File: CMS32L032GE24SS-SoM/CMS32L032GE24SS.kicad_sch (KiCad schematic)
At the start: 9 parts, among them J101 MCU Right Side, J102 MCU Left Side, U101 CMS32L032GE24SS

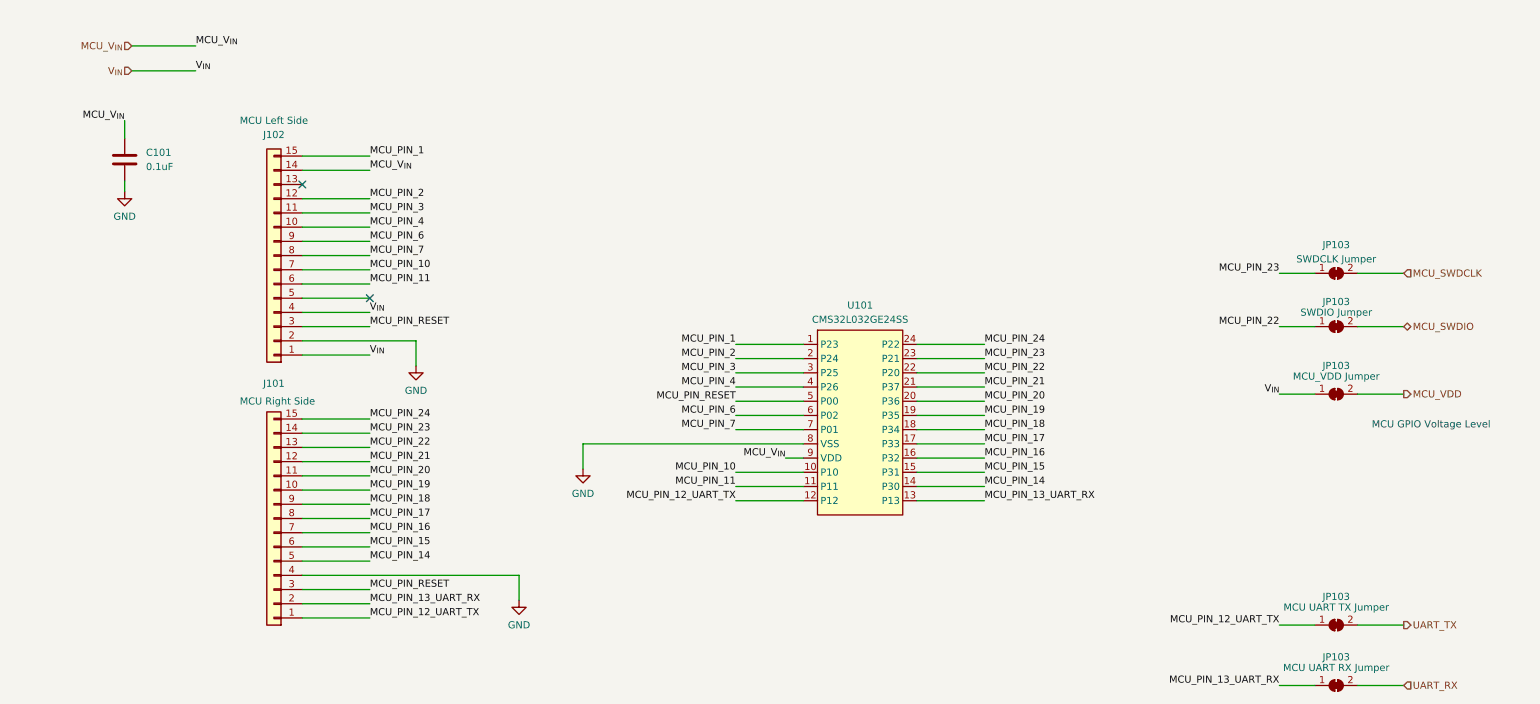
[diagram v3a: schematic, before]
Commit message: changed Power Source jumpers
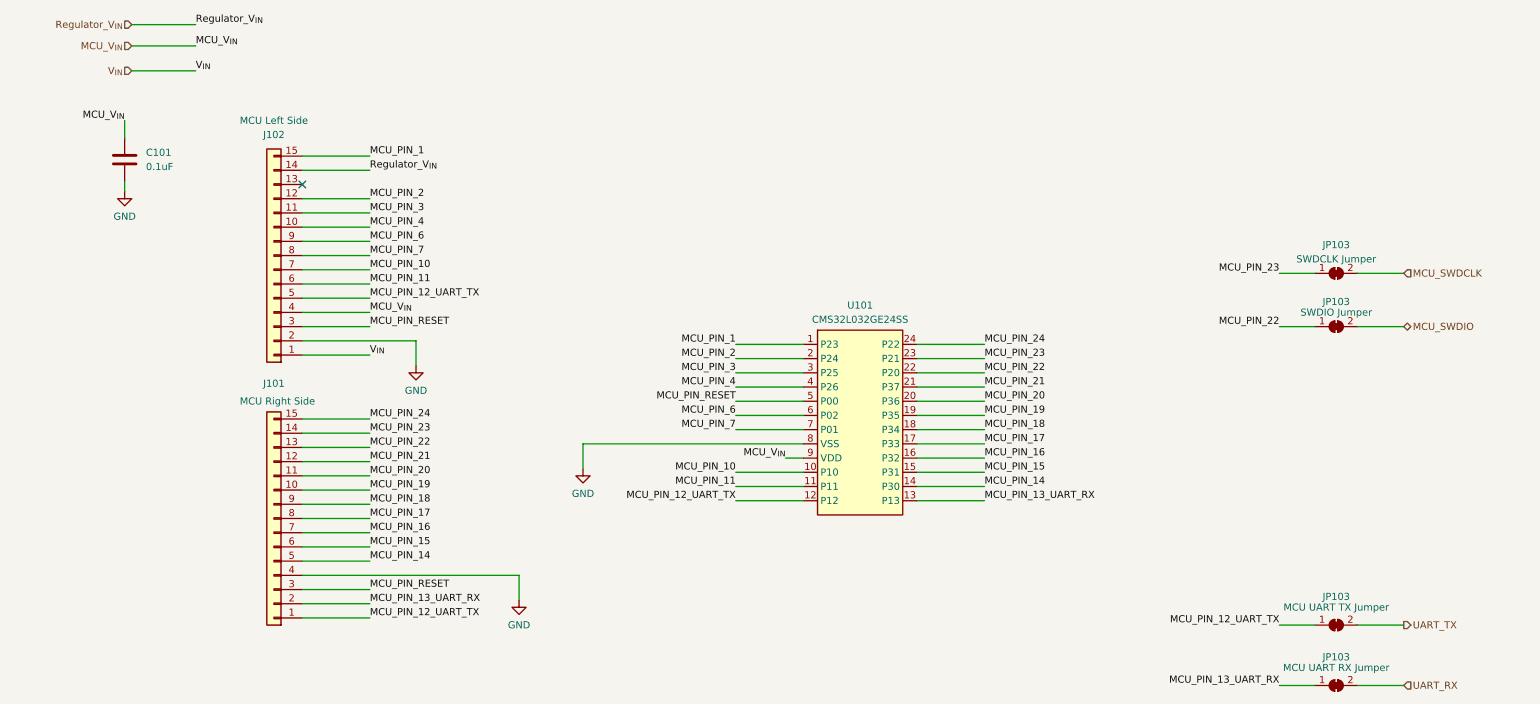
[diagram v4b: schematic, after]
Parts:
- removed JP103: MCU_VDD Jumper, Jumper:SolderJumper-2_P1.3mm_Bridged_RoundedPad1.0x1.5mm, symbol Jumper:SolderJumper_2_Bridged
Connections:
- net MCU_PIN_12_UART_TX: now also J102.5 (Pin_5)
- net MCU_V_{IN}: now also J102.4 (Pin_4); no longer J102.14 (Pin_14)
- net V_{IN}: no longer J102.4 (Pin_4)
- new net Regulator_V_{IN}: J102.14 (Pin_14)
- no-connect marks 2 -> 1
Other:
- note removed: "MCU GPIO Voltage Level"
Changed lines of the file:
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@@
 (kicad_sch (version 20230121) (generator eeschema)
   (paper "A4")
-  (no_connect (at 71.12 69.85))
   (no_connect (at 59.055 49.53))
   (wire (pts (xy 59.055 74.93) (xy 71.12 74.93))
@@
     (stroke (width 0) (type default))
   )
-  (wire (pts (xy 247.65 86.995) (xy 255.905 86.995))
-    (stroke (width 0) (type default))
-  )
   (wire (pts (xy 59.055 67.31) (xy 71.12 67.31))
     (stroke (width 0) (type default))
@@
     (stroke (width 0) (type default))
   )
+  (wire (pts (xy 28.575 20.955) (xy 40.005 20.955))
+    (stroke (width 0) (type default))
+  )
   (wire (pts (xy 59.055 72.39) (xy 71.12 72.39))
     (stroke (width 0) (type default))
@@
     (stroke (width 0) (type default))
   )
-  (wire (pts (xy 233.68 86.995) (xy 240.03 86.995))
-    (stroke (width 0) (type default))
-  )
   (wire (pts (xy 168.91 83.185) (xy 180.975 83.185))
     (stroke (width 0) (type default))
@@
     (stroke (width 0) (type default))
   )
-  (text "MCU GPIO Voltage Level" (at 250.19 93.345 0)
-    (effects (font (size 1.27 1.27)) (justify left bottom))
-  )
   (label "MCU_PIN_3" (at 136.525 83.185 180) (fields_autoplaced)
     (effects (font (size 1.27 1.27)) (justify right bottom))
@@
     (effects (font (size 1.27 1.27)) (justify left bottom))
   )
-  (label "V_{IN}" (at 233.68 86.995 180) (fields_autoplaced)
-    (effects (font (size 1.27 1.27)) (justify right bottom))
-  )
   (label "MCU_PIN_7" (at 71.12 62.23 0) (fields_autoplaced)
     (effects (font (size 1.27 1.27)) (justify left bottom))
@@
     (effects (font (size 1.27 1.27)) (justify left bottom))
   )
-  (label "V_{IN}" (at 71.12 72.39 0) (fields_autoplaced)
+  (label "MCU_V_{IN}" (at 71.12 72.39 0) (fields_autoplaced)
     (effects (font (size 1.27 1.27)) (justify left bottom))
   )
@@
     (effects (font (size 1.27 1.27)) (justify left bottom))
   )
+  (label "Regulator_V_{IN}" (at 40.005 20.955 0) (fields_autoplaced)
+    (effects (font (size 1.27 1.27)) (justify left bottom))
+  )
   (label "MCU_PIN_22" (at 180.975 83.185 0) (fields_autoplaced)
     (effects (font (size 1.27 1.27)) (justify left bottom))
@@
     (effects (font (size 1.27 1.27)) (justify right bottom))
   )
-  (label "MCU_V_{IN}" (at 71.12 46.99 0) (fields_autoplaced)
+  (label "Regulator_V_{IN}" (at 71.12 46.99 0) (fields_autoplaced)
     (effects (font (size 1.27 1.27)) (justify left bottom))
   )
@@
   )
   (label "MCU_PIN_21" (at 71.12 99.06 0) (fields_autoplaced)
+    (effects (font (size 1.27 1.27)) (justify left bottom))
+  )
+  (label "MCU_PIN_12_UART_TX" (at 71.12 69.85 0) (fields_autoplaced)
     (effects (font (size 1.27 1.27)) (justify left bottom))
   )
@@
     (effects (font (size 1.27 1.27)) (justify left))
   )
-  (hierarchical_label "MCU_VDD" (shape output) (at 255.905 86.995 0) (fields_autoplaced)
-    (effects (font (size 1.27 1.27)) (justify left))
-  )
   (hierarchical_label "UART_RX" (shape input) (at 255.905 139.065 0) (fields_autoplaced)
     (effects (font (size 1.27 1.27)) (justify left))
@@
   (hierarchical_label "MCU_SWDCLK" (shape input) (at 255.905 65.405 0) (fields_autoplaced)
     (effects (font (size 1.27 1.27)) (justify left))
+  )
+  (hierarchical_label "Regulator_V_{IN}" (shape input) (at 28.575 20.955 180) (fields_autoplaced)
+    (effects (font (size 1.27 1.27)) (justify right))
   )
   (hierarchical_label "V_{IN}" (shape input) (at 28.575 29.21 180) (fields_autoplaced)
@@
       (effects (font (size 1.27 1.27)) hide)
     )
+    (property "Description" "" (at 27.305 45.085 0)
+      (effects (font (size 1.27 1.27)) hide)
+    )
+    (property "LCSC" "" (at 27.305 45.085 0)
+      (effects (font (size 1.27 1.27)) hide)
+    )
+    (property "Vendor" "" (at 27.305 45.085 0)
+      (effects (font (size 1.27 1.27)) hide)
+    )
+    (property "Vendor Model" "" (at 27.305 45.085 0)
+      (effects (font (size 1.27 1.27)) hide)
+    )
     (pin "1")
     (pin "2")
@@
       (effects (font (size 1.27 1.27)) hide)
     )
+    (property "Description" "" (at 243.84 74.93 0)
+      (effects (font (size 1.27 1.27)) hide)
+    )
+    (property "LCSC" "" (at 243.84 74.93 0)
+      (effects (font (size 1.27 1.27)) hide)
+    )
+    (property "Vendor" "" (at 243.84 74.93 0)
+      (effects (font (size 1.27 1.27)) hide)
+    )
+    (property "Vendor Model" "" (at 243.84 74.93 0)
+      (effects (font (size 1.27 1.27)) hide)
+    )
     (pin "1")
     (pin "2")
@@
     )
     (property "Datasheet" "~" (at 53.975 109.22 0)
+      (effects (font (size 1.27 1.27)) hide)
+    )
+    (property "Description" "" (at 53.975 109.22 0)
+      (effects (font (size 1.27 1.27)) hide)
+    )
+    (property "LCSC" "" (at 53.975 109.22 0)
+      (effects (font (size 1.27 1.27)) hide)
+    )
+    (property "Vendor" "" (at 53.975 109.22 0)
+      (effects (font (size 1.27 1.27)) hide)
+    )
+    (property "Vendor Model" "" (at 53.975 109.22 0)
       (effects (font (size 1.27 1.27)) hide)
     )
@@
     )
     (property "Datasheet" "https://www.mcu.com.cn/uploads/img1/tupian/CMS32L032%20Datasheet_V1.0.1.pdf" (at 161.29 116.205 0)
+      (effects (font (size 1.27 1.27)) hide)
+    )
+    (property "Description" "" (at 158.75 90.805 0)
+      (effects (font (size 1.27 1.27)) hide)
+    )
+    (property "LCSC" "" (at 158.75 90.805 0)
+      (effects (font (size 1.27 1.27)) hide)
+    )
+    (property "Vendor" "" (at 158.75 90.805 0)
+      (effects (font (size 1.27 1.27)) hide)
+    )
+    (property "Vendor Model" "" (at 158.75 90.805 0)
       (effects (font (size 1.27 1.27)) hide)
     )
@@
       (effects (font (size 1.27 1.27)) hide)
     )
+    (property "Description" "" (at 243.84 65.405 0)
+      (effects (font (size 1.27 1.27)) hide)
+    )
+    (property "LCSC" "" (at 243.84 65.405 0)
+      (effects (font (size 1.27 1.27)) hide)
+    )
+    (property "Vendor" "" (at 243.84 65.405 0)
+      (effects (font (size 1.27 1.27)) hide)
+    )
+    (property "Vendor Model" "" (at 243.84 65.405 0)
+      (effects (font (size 1.27 1.27)) hide)
+    )
     (pin "1")
     (pin "2")
@@
       (effects (font (size 1.27 1.27)) hide)
     )
+    (property "Description" "" (at 243.84 128.27 0)
+      (effects (font (size 1.27 1.27)) hide)
+    )
+    (property "LCSC" "" (at 243.84 128.27 0)
+      (effects (font (size 1.27 1.27)) hide)
+    )
+    (property "Vendor" "" (at 243.84 128.27 0)
+      (effects (font (size 1.27 1.27)) hide)
+    )
+    (property "Vendor Model" "" (at 243.84 128.27 0)
+      (effects (font (size 1.27 1.27)) hide)
+    )
     (pin "1")
     (pin "2")
@@
         (path "/c0ebcd8e-c90a-40d9-842d-ee55e79d6adf/29b9f769-3d76-4235-af85-93dac208c17b"
           (reference "JP204") (unit 1)
-        )
-      )
-    )
-  )
-  (symbol (lib_id "Jumper:SolderJumper_2_Bridged") (at 243.84 86.995 0) (unit 1)
-    (in_bom yes) (on_board yes) (dnp no)
-    (property "Reference" "JP103" (at 243.84 81.915 0)
-      (effects (font (size 1.27 1.27)))
-    )
-    (property "Value" "MCU_VDD Jumper" (at 243.84 83.82 0)
-      (effects (font (size 1.27 1.27)))
-    )
-    (property "Footprint" "Jumper:SolderJumper-2_P1.3mm_Bridged_RoundedPad1.0x1.5mm" (at 243.84 86.995 0)
-      (effects (font (size 1.27 1.27)) hide)
-    )
-    (property "Datasheet" "~" (at 243.84 86.995 0)
-      (effects (font (size 1.27 1.27)) hide)
-    )
-    (pin "1")
-    (pin "2")
-    (instances
-      (project "CMS32L032GE24SS-SoM"
-        (path "/c0ebcd8e-c90a-40d9-842d-ee55e79d6adf"
-          (reference "JP103") (unit 1)
-        )
-        (path "/c0ebcd8e-c90a-40d9-842d-ee55e79d6adf/29b9f769-3d76-4235-af85-93dac208c17b"
-          (reference "JP203") (unit 1)
         )
       )
@@
     )
     (property "Datasheet" "~" (at 53.975 62.23 0)
+      (effects (font (size 1.27 1.27)) hide)
+    )
+    (property "Description" "" (at 53.975 62.23 0)
+      (effects (font (size 1.27 1.27)) hide)
+    )
+    (property "LCSC" "" (at 53.975 62.23 0)
+      (effects (font (size 1.27 1.27)) hide)
+    )
+    (property "Vendor" "" (at 53.975 62.23 0)
+      (effects (font (size 1.27 1.27)) hide)
+    )
+    (property "Vendor Model" "" (at 53.975 62.23 0)
       (effects (font (size 1.27 1.27)) hide)
     )
@@
       (effects (font (size 1.27 1.27)) hide)
     )
+    (property "Description" "" (at 243.84 139.065 0)
+      (effects (font (size 1.27 1.27)) hide)
+    )
+    (property "LCSC" "" (at 243.84 139.065 0)
+      (effects (font (size 1.27 1.27)) hide)
+    )
+    (property "Vendor" "" (at 243.84 139.065 0)
+      (effects (font (size 1.27 1.27)) hide)
+    )
+    (property "Vendor Model" "" (at 243.84 139.065 0)
+      (effects (font (size 1.27 1.27)) hide)
+    )

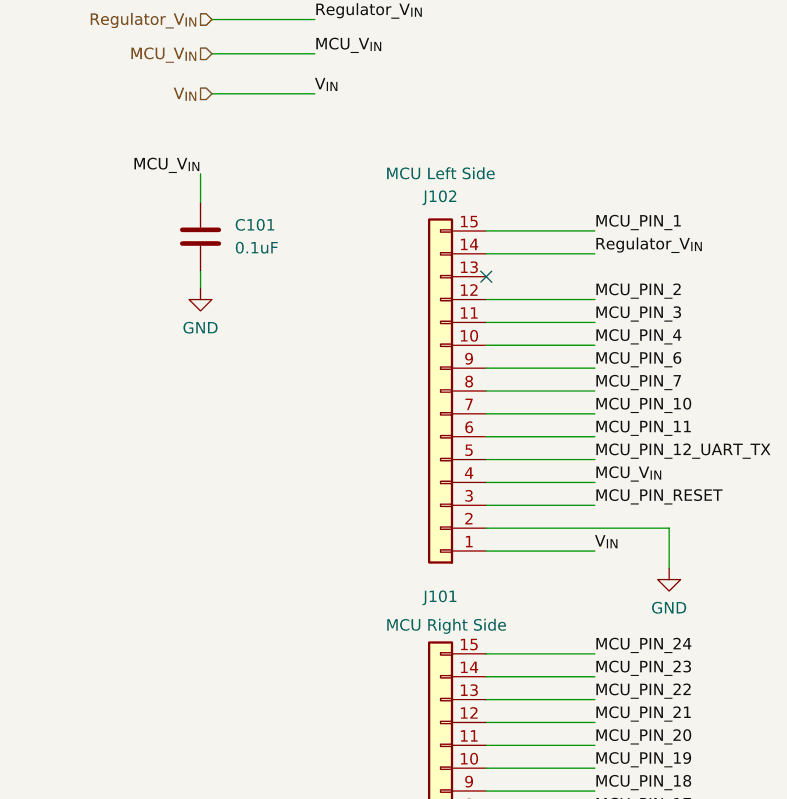
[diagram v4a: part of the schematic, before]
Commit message: updated Part number in LCSC
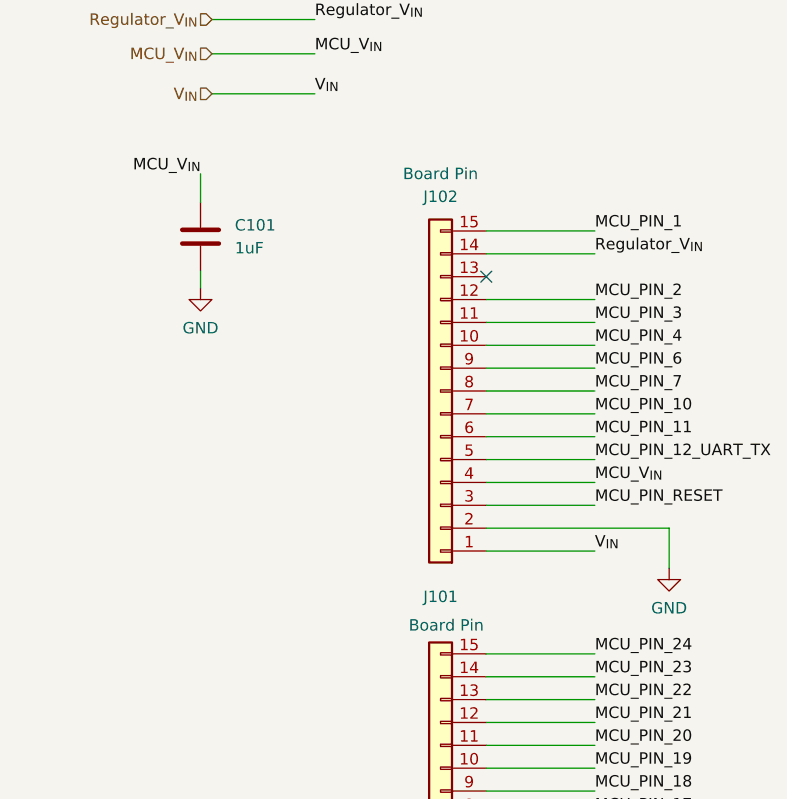
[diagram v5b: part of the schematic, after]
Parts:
- C101: value 0.1uF -> 1uF; LCSC (none) -> C116352; Vendor (none) -> SAMSUNG(三星); Vendor Model (none) -> CL21B105KAFNNNE
- J101: value MCU Right Side -> Board Pin; LCSC (none) -> C124373; Vendor (none) -> Ckmtw(灿科盟); Vendor Model (none) -> B-2100S15P-A110
- J102: value MCU Left Side -> Board Pin; LCSC (none) -> C124373; Vendor (none) -> Ckmtw(灿科盟); Vendor Model (none) -> B-2100S15P-A110
- JP103: now left out of the parts list
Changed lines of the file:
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@@
       (effects (font (size 1.27 1.27)) (justify left))
     )
-    (property "Value" "0.1uF" (at 31.115 46.355 0)
+    (property "Value" "1uF" (at 31.115 46.355 0)
       (effects (font (size 1.27 1.27)) (justify left))
     )
@@
       (effects (font (size 1.27 1.27)) hide)
     )
-    (property "Description" "" (at 27.305 45.085 0)
-      (effects (font (size 1.27 1.27)) hide)
-    )
-    (property "LCSC" "" (at 27.305 45.085 0)
-      (effects (font (size 1.27 1.27)) hide)
-    )
-    (property "Vendor" "" (at 27.305 45.085 0)
-      (effects (font (size 1.27 1.27)) hide)
-    )
-    (property "Vendor Model" "" (at 27.305 45.085 0)
+    (property "Description" "容值: 1uF 精度: ±10% 额定电压: 25V 材质(温度系数): X7R 材质：X7R" (at 27.305 45.085 0)
+      (effects (font (size 1.27 1.27)) hide)
+    )
+    (property "LCSC" "C116352" (at 27.305 45.085 0)
+      (effects (font (size 1.27 1.27)) hide)
+    )
+    (property "Vendor" "SAMSUNG(三星)" (at 27.305 45.085 0)
+      (effects (font (size 1.27 1.27)) hide)
+    )
+    (property "Vendor Model" "CL21B105KAFNNNE" (at 27.305 45.085 0)
       (effects (font (size 1.27 1.27)) hide)
     )
@@
   )
   (symbol (lib_id "Jumper:SolderJumper_2_Bridged") (at 243.84 74.93 0) (unit 1)
-    (in_bom yes) (on_board yes) (dnp no)
+    (in_bom no) (on_board yes) (dnp no)
     (property "Reference" "JP103" (at 243.84 70.485 0)
       (effects (font (size 1.27 1.27)))
@@
       (effects (font (size 1.27 1.27)))
     )
-    (property "Value" "MCU Right Side" (at 54.61 88.265 0)
+    (property "Value" "Board Pin" (at 54.61 88.265 0)
       (effects (font (size 1.27 1.27)))
     )
@@
       (effects (font (size 1.27 1.27)) hide)
     )
-    (property "Description" "" (at 53.975 109.22 0)
-      (effects (font (size 1.27 1.27)) hide)
-    )
-    (property "LCSC" "" (at 53.975 109.22 0)
-      (effects (font (size 1.27 1.27)) hide)
-    )
-    (property "Vendor" "" (at 53.975 109.22 0)
-      (effects (font (size 1.27 1.27)) hide)
-    )
-    (property "Vendor Model" "" (at 53.975 109.22 0)
+    (property "Description" "排数: 单排 总PIN位数: 15 总PIN位数: 15P 间距: 2.54mm 插针结构: 1x15P 行距: - 安装类型: 直插 圆针/方针: - 额定电流: - 额定电压: - 配合针长度: 6mm 塑高: 2.54mm " (at 53.975 109.22 0)
+      (effects (font (size 1.27 1.27)) hide)
+    )
+    (property "LCSC" "C124373" (at 53.975 109.22 0)
+      (effects (font (size 1.27 1.27)) hide)
+    )
+    (property "Vendor" "Ckmtw(灿科盟)" (at 53.975 109.22 0)
+      (effects (font (size 1.27 1.27)) hide)
+    )
+    (property "Vendor Model" "B-2100S15P-A110" (at 53.975 109.22 0)
       (effects (font (size 1.27 1.27)) hide)
     )
@@
   )
   (symbol (lib_id "Jumper:SolderJumper_2_Bridged") (at 243.84 65.405 0) (unit 1)
-    (in_bom yes) (on_board yes) (dnp no)
+    (in_bom no) (on_board yes) (dnp no)
     (property "Reference" "JP103" (at 243.84 60.325 0)
       (effects (font (size 1.27 1.27)))
@@
   )
   (symbol (lib_id "Jumper:SolderJumper_2_Bridged") (at 243.84 128.27 0) (unit 1)
-    (in_bom yes) (on_board yes) (dnp no)
+    (in_bom no) (on_board yes) (dnp no)
     (property "Reference" "JP103" (at 243.84 123.19 0)
       (effects (font (size 1.27 1.27)))
@@
       (effects (font (size 1.27 1.27)))
     )
-    (property "Value" "MCU Left Side" (at 53.975 38.1 0)
+    (property "Value" "Board Pin" (at 53.975 38.1 0)
       (effects (font (size 1.27 1.27)))
     )
@@
       (effects (font (size 1.27 1.27)) hide)
     )
-    (property "Description" "" (at 53.975 62.23 0)
-      (effects (font (size 1.27 1.27)) hide)
-    )
-    (property "LCSC" "" (at 53.975 62.23 0)
-      (effects (font (size 1.27 1.27)) hide)
-    )
-    (property "Vendor" "" (at 53.975 62.23 0)
-      (effects (font (size 1.27 1.27)) hide)
-    )
-    (property "Vendor Model" "" (at 53.975 62.23 0)
+    (property "Description" "排数: 单排 总PIN位数: 15 总PIN位数: 15P 间距: 2.54mm 插针结构: 1x15P 行距: - 安装类型: 直插 圆针/方针: - 额定电流: - 额定电压: - 配合针长度: 6mm 塑高: 2.54mm " (at 53.975 62.23 0)
+      (effects (font (size 1.27 1.27)) hide)
+    )
+    (property "LCSC" "C124373" (at 53.975 62.23 0)
+      (effects (font (size 1.27 1.27)) hide)
+    )
+    (property "Vendor" "Ckmtw(灿科盟)" (at 53.975 62.23 0)
+      (effects (font (size 1.27 1.27)) hide)
+    )
+    (property "Vendor Model" "B-2100S15P-A110" (at 53.975 62.23 0)
       (effects (font (size 1.27 1.27)) hide)
     )
@@
   )
   (symbol (lib_id "Jumper:SolderJumper_2_Bridged") (at 243.84 139.065 0) (unit 1)
-    (in_bom yes) (on_board yes) (dnp no)
+    (in_bom no) (on_board yes) (dnp no)
     (property "Reference" "JP103" (at 243.84 133.985 0)
       (effects (font (size 1.27 1.27)))
